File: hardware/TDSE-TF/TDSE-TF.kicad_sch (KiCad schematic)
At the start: 30 parts, among them J1 Sensor nivel de agua, J10 CN10, J2 Tira LED, J3 +5VCC entrada, J5 Bomba, J6 Sensor nivel de luz, J7 CN7, J8 Sensor humedad de suelo, J9 Conector LCD16x02, Q1 IRLZ44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

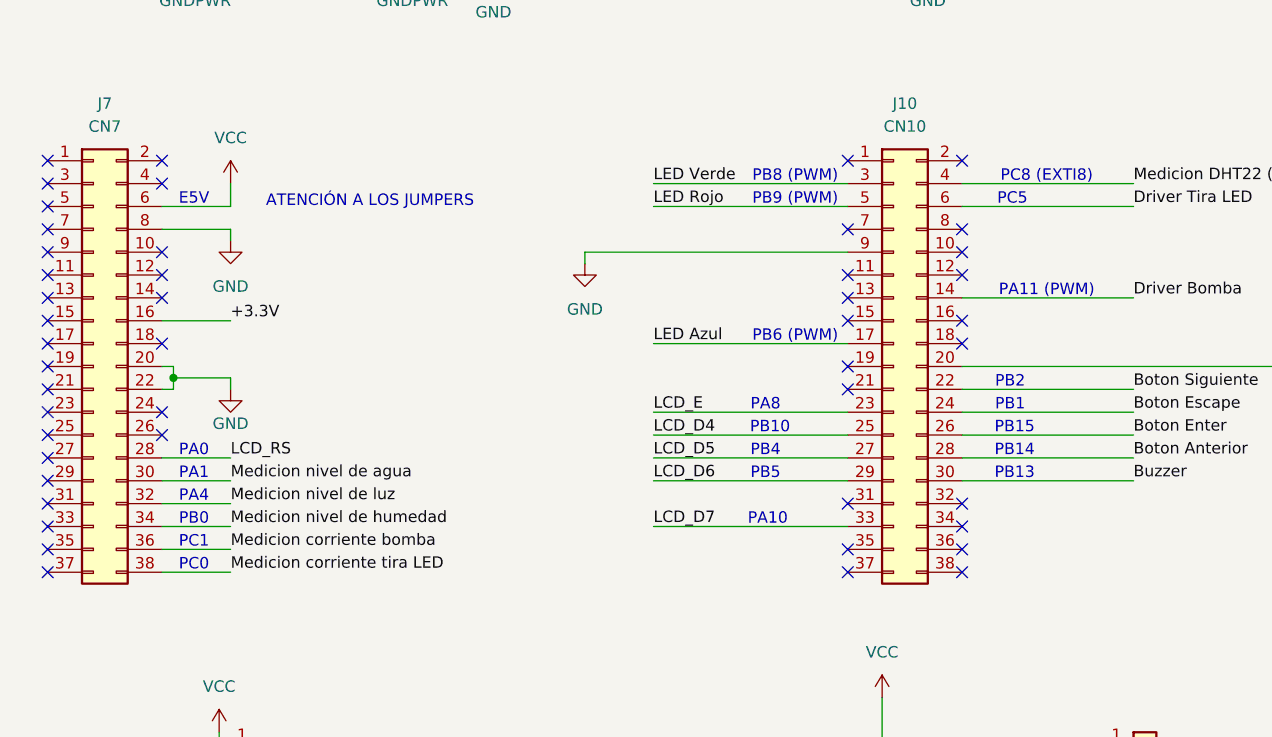
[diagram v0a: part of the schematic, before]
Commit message: Finalizado modo falla y actualizacion de PCB
Se terminó el modo falla
Se ajustaron tamaños y ubicaciones de etiquetas para el FFab del PCB y se corrigió la ubicacion del DHT22
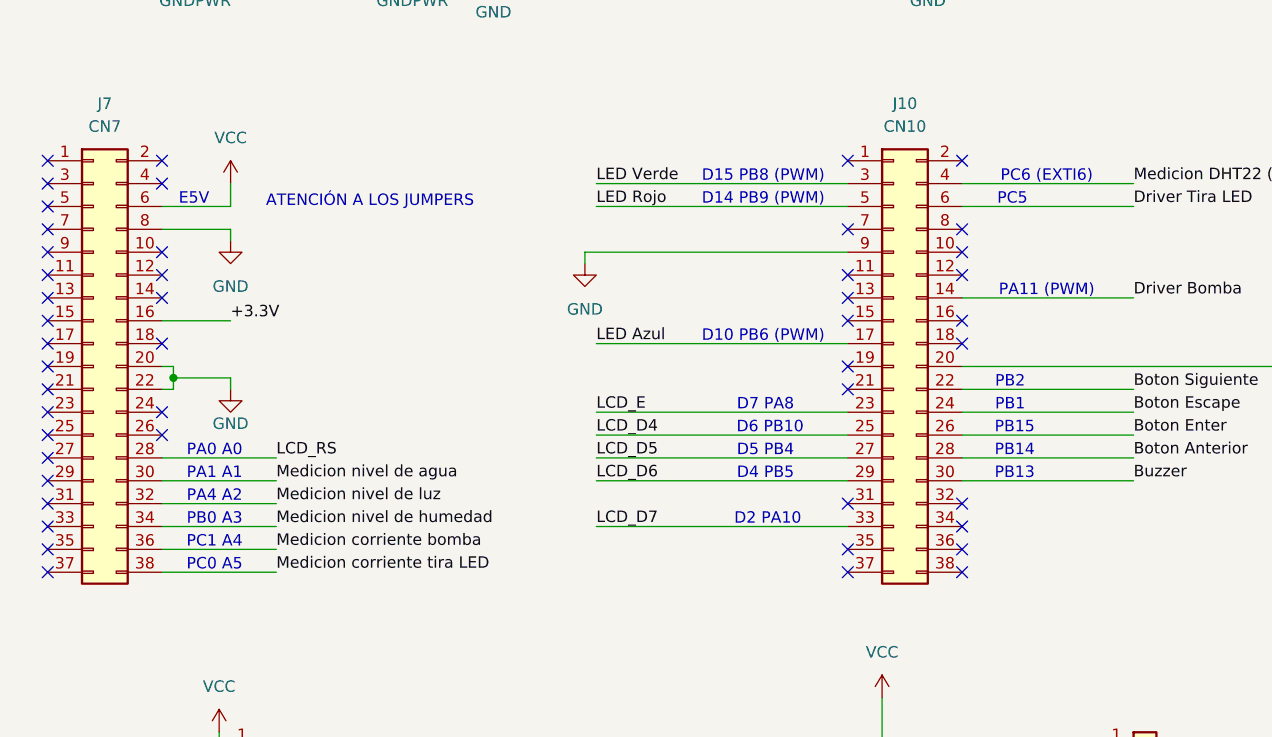
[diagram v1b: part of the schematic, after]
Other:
- note added: "D10 PB6 (PWM)"
- note added: "D14 PB9 (PWM)"
- note added: "D15 PB8 (PWM)"
- note added: "D2 PA10"
- note added: "D4 PB5"
- note added: "D5 PB4"
- note added: "D6 PB10"
- note added: "D7 PA8"
- note added: "PA0 A0"
- note added: "PA1 A1"
- note added: "PA4 A2"
- note added: "PB0 A3"
- note added: "PC0 A5"
- note added: "PC1 A4"
- note added: "PC6 (EXTI6)"
- note removed: "PA0"
- note removed: "PA1"
- note removed: "PA10"
- note removed: "PA4"
- note removed: "PA8"
- note removed: "PB0"
- note removed: "PB10"
- note removed: "PB4"
- note removed: "PB5"
- note removed: "PB6 (PWM)"
- note removed: "PB8 (PWM)"
- note removed: "PB9 (PWM)"
- note removed: "PC0"
- note removed: "PC1"
- note removed: "PC8 (EXTI8)"
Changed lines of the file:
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@@
 		(comment 1 "Carrizo Ezequiel Ignacio, Gonzalez Bigliardi Iñaki, Juncal Franco Mariano")
 	)
-	(text "PB4"
+	(text "D5 PB4"
 		(exclude_from_sim no)
 		(at 108.966 88.138 0)
@@
 		)
 	)
-	(text "PB5\n"
+	(text "D4 PB5\n"
 		(exclude_from_sim no)
 		(at 108.966 90.678 0)
@@
 		)
 	)
-	(text "PC0"
-		(exclude_from_sim no)
-		(at 45.466 100.838 0)
+	(text "PC0 A5"
+		(exclude_from_sim no)
+		(at 47.752 100.838 0)
 		(effects
 			(font
@@
 		)
 	)
-	(text "PA1"
-		(exclude_from_sim no)
-		(at 45.466 90.678 0)
+	(text "PA1 A1"
+		(exclude_from_sim no)
+		(at 47.752 90.678 0)
 		(effects
 			(font
@@
 		)
 	)
-	(text "PB9 (PWM)"
-		(exclude_from_sim no)
-		(at 112.268 60.198 0)
+	(text "D14 PB9 (PWM)"
+		(exclude_from_sim no)
+		(at 108.712 60.198 0)
 		(effects
 			(font
@@
 		)
 	)
-	(text "PB8 (PWM)"
-		(exclude_from_sim no)
-		(at 112.268 57.658 0)
-		(effects
-			(font
-				(size 1.27 1.27)
-			)
-		)
-	)
-	(text "PC1"
-		(exclude_from_sim no)
-		(at 45.466 98.298 0)
+	(text "D15 PB8 (PWM)"
+		(exclude_from_sim no)
+		(at 108.712 57.658 0)
+		(effects
+			(font
+				(size 1.27 1.27)
+			)
+		)
+	)
+	(text "PC1 A4"
+		(exclude_from_sim no)
+		(at 47.752 98.298 0)
 		(effects
 			(font
@@
 		)
 	)
-	(text "PB0"
-		(exclude_from_sim no)
-		(at 45.466 95.758 0)
+	(text "PB0 A3"
+		(exclude_from_sim no)
+		(at 47.752 95.758 0)
 		(effects
 			(font
@@
 		)
 	)
-	(text "PA10"
+	(text "D2 PA10"
 		(exclude_from_sim no)
 		(at 109.22 95.758 0)
@@
 		)
 	)
-	(text "PA0"
-		(exclude_from_sim no)
-		(at 45.466 88.138 0)
-		(effects
-			(font
-				(size 1.27 1.27)
-			)
-		)
-	)
-	(text "PB10"
+	(text "PA0 A0"
+		(exclude_from_sim no)
+		(at 47.752 88.138 0)
+		(effects
+			(font
+				(size 1.27 1.27)
+			)
+		)
+	)
+	(text "D6 PB10"
 		(exclude_from_sim no)
 		(at 109.474 85.598 0)
@@
 		)
 	)
-	(text "PB6 (PWM)"
-		(exclude_from_sim no)
-		(at 112.268 75.438 0)
-		(effects
-			(font
-				(size 1.27 1.27)
-			)
-		)
-	)
-	(text "PA8"
+	(text "D10 PB6 (PWM)"
+		(exclude_from_sim no)
+		(at 108.712 75.438 0)
+		(effects
+			(font
+				(size 1.27 1.27)
+			)
+		)
+	)
+	(text "D7 PA8"
 		(exclude_from_sim no)
 		(at 108.966 83.058 0)
@@
 		)
 	)
-	(text "PA4"
-		(exclude_from_sim no)
-		(at 45.466 93.218 0)
+	(text "PA4 A2"
+		(exclude_from_sim no)
+		(at 47.752 93.218 0)
 		(effects
 			(font
@@
 		)
 	)
-	(text "PC8 (EXTI8)\n"
+	(text "PC6 (EXTI6)\n"
 		(exclude_from_sim no)
 		(at 140.208 57.658 0)
@@
 	(wire
 		(pts
+			(xy 90.17 91.44) (xy 118.11 91.44)
+		)
+		(stroke
+			(width 0)
+			(type default)
+		)
+	)
+	(wire
+		(pts
 			(xy 260.35 67.31) (xy 261.62 67.31)
 		)
@@
 	(wire
 		(pts
-			(xy 96.52 58.42) (xy 118.11 58.42)
+			(xy 90.17 86.36) (xy 118.11 86.36)
 		)
 		(stroke
@@
 	(wire
 		(pts
+			(xy 90.17 76.2) (xy 118.11 76.2)
+		)
+		(stroke
+			(width 0)
+			(type default)
+		)
+	)
+	(wire
+		(pts
 			(xy 88.9 67.31) (xy 88.9 66.04)
 		)
@@
 	(wire
 		(pts
+			(xy 90.17 88.9) (xy 118.11 88.9)
+		)
+		(stroke
+			(width 0)
+			(type default)
+		)
+	)
+	(wire
+		(pts
 			(xy 133.35 120.65) (xy 146.05 120.65)
 		)
@@
 	(wire
 		(pts
-			(xy 96.52 83.82) (xy 118.11 83.82)
-		)
-		(stroke
-			(width 0)
-			(type default)
-		)
-	)
-	(wire
-		(pts
 			(xy 261.62 116.84) (xy 261.62 123.19)
 		)
@@
 	(wire
 		(pts
-			(xy 41.91 99.06) (xy 49.53 99.06)
+			(xy 41.91 99.06) (xy 54.61 99.06)
 		)
 		(stroke
@@
 	(wire
 		(pts
-			(xy 41.91 101.6) (xy 49.53 101.6)
+			(xy 41.91 101.6) (xy 54.61 101.6)
 		)
 		(stroke
@@
 	(wire
 		(pts
-			(xy 41.91 88.9) (xy 49.53 88.9)
+			(xy 41.91 88.9) (xy 54.61 88.9)
 		)
 		(stroke
@@
 	(wire
 		(pts
-			(xy 41.91 96.52) (xy 49.53 96.52)
+			(xy 41.91 96.52) (xy 54.61 96.52)
 		)
 		(stroke
@@
 	(wire
 		(pts
-			(xy 96.52 91.44) (xy 118.11 91.44)
+			(xy 90.17 58.42) (xy 118.11 58.42)
 		)
 		(stroke
@@
 	(wire
 		(pts
-			(xy 41.91 93.98) (xy 49.53 93.98)
+			(xy 41.91 93.98) (xy 54.61 93.98)
 		)
 		(stroke
@@
 	(wire
 		(pts
+			(xy 90.17 83.82) (xy 118.11 83.82)
+		)
+		(stroke
+			(width 0)
+			(type default)
+		)
+	)
+	(wire
+		(pts
 			(xy 130.81 88.9) (xy 149.86 88.9)
 		)
@@
 	(wire
 		(pts
+			(xy 90.17 60.96) (xy 118.11 60.96)
+		)
+		(stroke
+			(width 0)
+			(type default)
+		)
+	)
+	(wire
+		(pts
 			(xy 163.83 29.21) (xy 187.96 29.21)
 		)
@@
 	(wire
 		(pts
-			(xy 96.52 96.52) (xy 118.11 96.52)
-		)
-		(stroke
-			(width 0)
-			(type default)
-		)
-	)
-	(wire
-		(pts
 			(xy 207.01 147.32) (xy 207.01 149.86)
 		)
@@
 	(wire
 		(pts
-			(xy 96.52 88.9) (xy 118.11 88.9)
-		)
-		(stroke
-			(width 0)
-			(type default)
-		)
-	)
-	(wire
-		(pts
 			(xy 41.91 63.5) (xy 49.53 63.5)
 		)
@@
 	(wire
 		(pts
-			(xy 96.52 60.96) (xy 118.11 60.96)
-		)
-		(stroke
-			(width 0)
-			(type default)
-		)
-	)
-	(wire
-		(pts
 			(xy 134.62 156.21) (xy 146.05 156.21)
 		)
@@
 	(wire
 		(pts
-			(xy 41.91 91.44) (xy 49.53 91.44)
+			(xy 41.91 91.44) (xy 54.61 91.44)
 		)
 		(stroke
@@
 	(wire
 		(pts
-			(xy 96.52 76.2) (xy 118.11 76.2)
-		)
-		(stroke
-			(width 0)
-			(type default)
-		)
-	)
-	(wire
-		(pts
-			(xy 96.52 86.36) (xy 118.11 86.36)
+			(xy 90.17 96.52) (xy 118.11 96.52)
 		)
 		(stroke
@@
 	)
 	(label "LED Rojo"
-		(at 96.52 60.96 0)
+		(at 90.17 60.96 0)
 		(effects
 			(font
@@
 	)
 	(label "LCD_D5"
-		(at 96.52 88.9 0)
+		(at 90.17 88.9 0)
 		(effects
 			(font
@@
 	)
 	(label "LCD_D6"
-		(at 96.52 91.44 0)
+		(at 90.17 91.44 0)
 		(effects
 			(font
@@
 	)
 	(label "Medicion nivel de humedad"
-		(at 49.53 96.52 0)
+		(at 54.61 96.52 0)
 		(effects
 			(font
@@
 	)
 	(label "Medicion nivel de luz"
-		(at 49.53 93.98 0)
+		(at 54.61 93.98 0)
 		(effects
 			(font
@@
 	)
 	(label "LCD_E"
-		(at 96.52 83.82 0)
+		(at 90.17 83.82 0)
 		(effects
 			(font
@@
 	)
 	(label "LED Verde"
-		(at 96.52 58.42 0)
+		(at 90.17 58.42 0)
 		(effects
 			(font
@@
 	)
 	(label "Medicion nivel de agua"
-		(at 49.53 91.44 0)
+		(at 54.61 91.44 0)
 		(effects
 			(font
@@
 	)
 	(label "LED Azul"
-		(at 96.52 76.2 0)
+		(at 90.17 76.2 0)
 		(effects
 			(font
@@
 	)
 	(label "LCD_D4"
-		(at 96.52 86.36 0)
+		(at 90.17 86.36 0)
 		(effects
 			(font
@@
 	)
 	(label "Medicion corriente tira LED"
-		(at 49.53 101.6 0)
+		(at 54.61 101.6 0)
 		(effects
 			(font
@@
 	)
 	(label "Medicion corriente bomba"
-		(at 49.53 99.06 0)
+		(at 54.61 99.06 0)
 		(effects
 			(font
@@
 	)
 	(label "LCD_D7"
-		(at 96.52 96.52 0)
+		(at 90.17 96.52 0)
 		(effects
 			(font
@@
 	)
 	(label "LCD_RS"
-		(at 49.53 88.9 0)
-		(effects
-			(font
+		(at 54.61 88.9 0)
+		(effects
+			(font
